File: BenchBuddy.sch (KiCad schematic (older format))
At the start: 0 parts

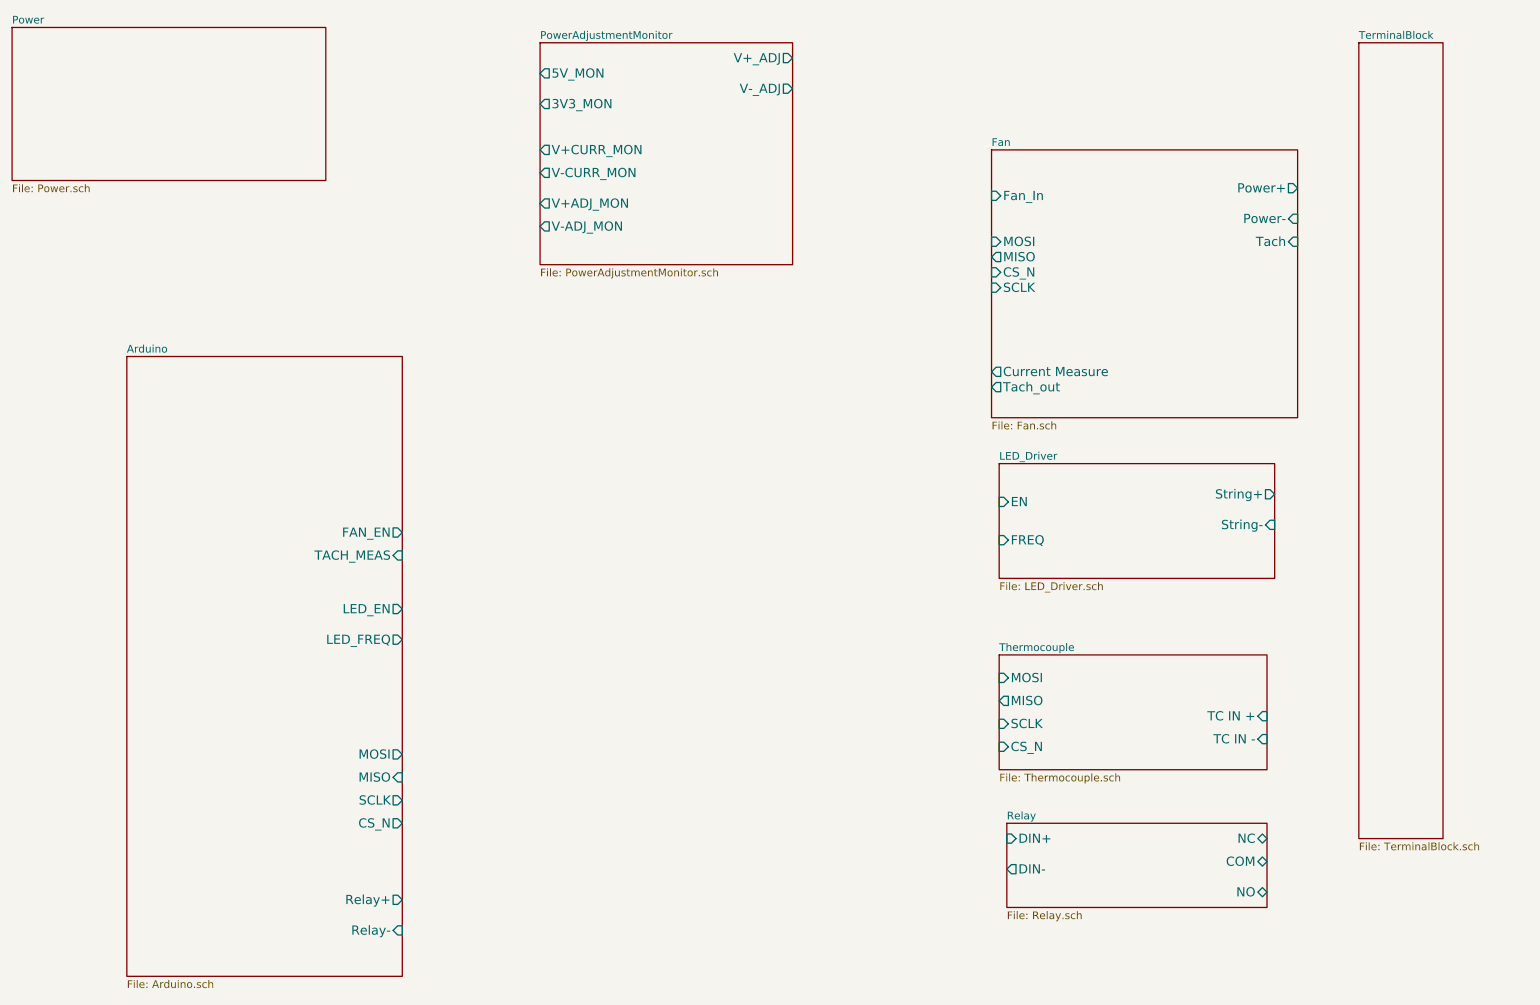
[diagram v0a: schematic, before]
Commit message: Changes up to and including Arduino module
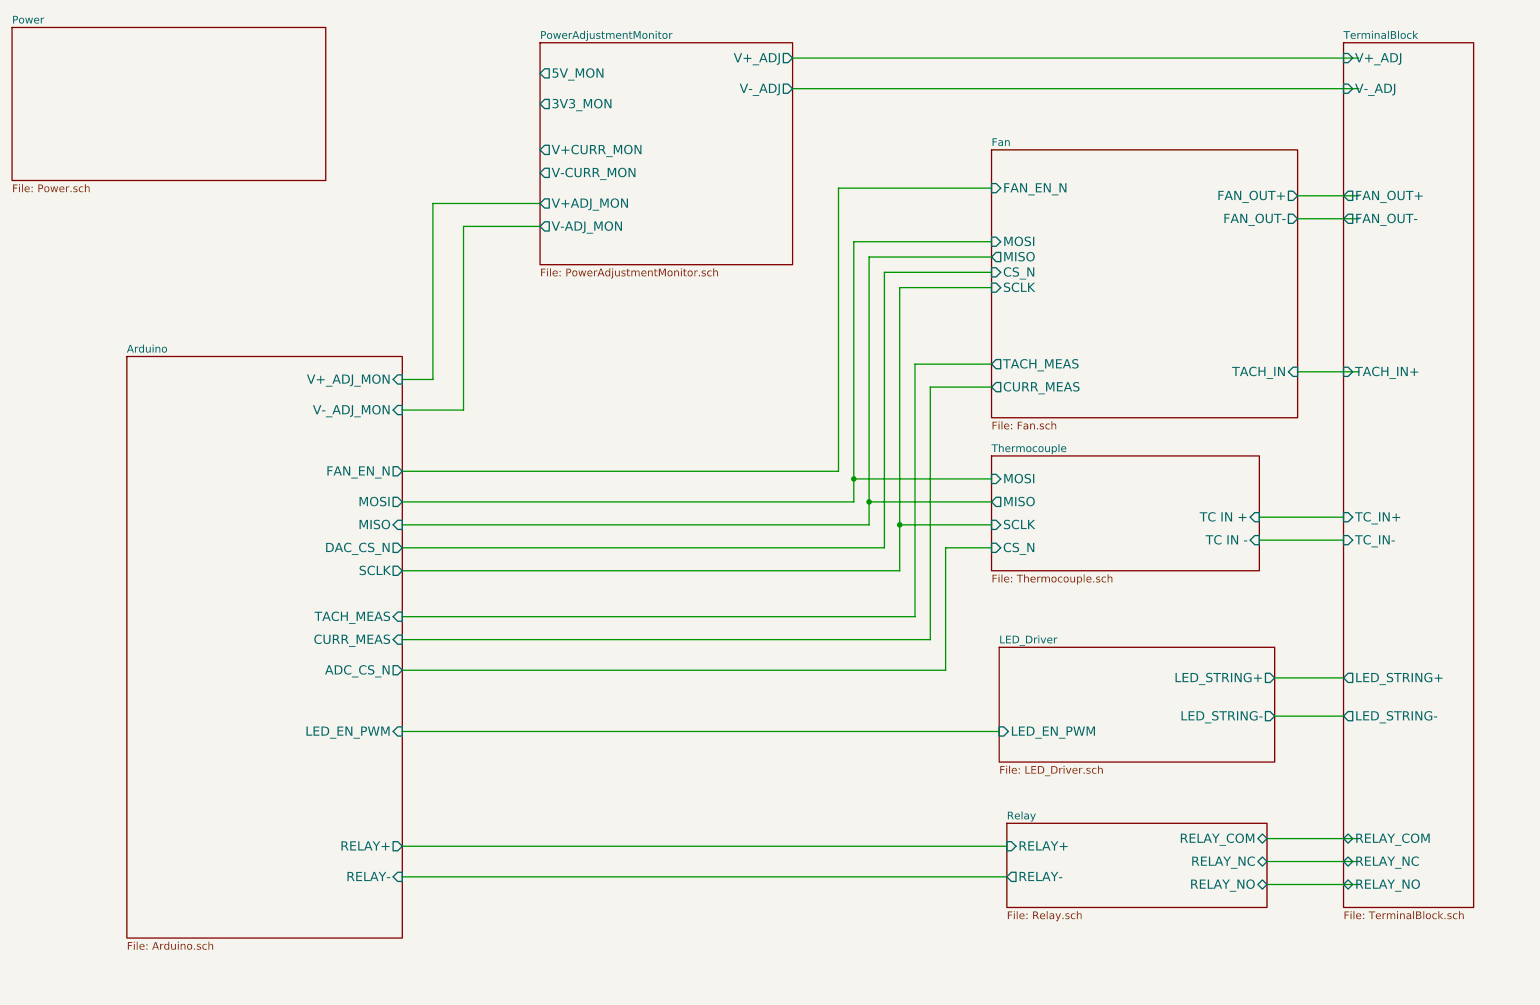
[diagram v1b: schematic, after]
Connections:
- wire segments 0 -> 48
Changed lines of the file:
@@
 LIBS:valves
 LIBS:BencyBuddy
+LIBS:arduino_shieldsNCL
 LIBS:BenchBuddy-cache
 EELAYER 27 0
@@
 Sheet 1 9
 Title ""
-Date "9 feb 2014"
+Date "12 feb 2014"
 Rev ""
 Comp ""
@@
 $EndDescr
 $Sheet
-S 1850 3200 1800 4050
+S 1850 3200 1800 3800
 U 52EF15C4
 F0 "Arduino" 50
 F1 "Arduino.sch" 50
-F2 "Relay+" O R 3650 6750 60
-F3 "Relay-" I R 3650 6950 60
-F4 "MOSI" O R 3650 5800 60
-F5 "MISO" I R 3650 5950 60
-F6 "SCLK" O R 3650 6100 60
-F7 "CS_N" O R 3650 6250 60
-F8 "LED_EN" O R 3650 4850 60
-F9 "LED_FREQ" O R 3650 5050 60
-F10 "FAN_EN" O R 3650 4350 60
-F11 "TACH_MEAS" I R 3650 4500 60
+F2 "RELAY+" O R 3650 6400 60
+F3 "RELAY-" I R 3650 6600 60
+F4 "MOSI" O R 3650 4150 60
+F5 "MISO" I R 3650 4300 60
+F6 "SCLK" O R 3650 4600 60
+F7 "TACH_MEAS" I R 3650 4900 60
+F8 "FAN_EN_N" O R 3650 3950 60
+F9 "CURR_MEAS" I R 3650 5050 60
+F10 "V+_ADJ_MON" I R 3650 3350 60
+F11 "V-_ADJ_MON" I R 3650 3550 60
+F12 "LED_EN_PWM" I R 3650 5650 60
+F13 "DAC_CS_N" O R 3650 4450 60
+F14 "ADC_CS_N" O R 3650 5250 60
 $EndSheet
 $Sheet
@@
 F0 "Relay" 50
 F1 "Relay.sch" 50
-F2 "DIN+" I L 7600 6350 60
-F3 "DIN-" O L 7600 6550 60
-F4 "NC" B R 9300 6350 60
-F5 "NO" B R 9300 6700 60
-F6 "COM" B R 9300 6500 60
+F2 "RELAY_NC" B R 9300 6500 60
+F3 "RELAY_NO" B R 9300 6650 60
+F4 "RELAY_COM" B R 9300 6350 60
+F5 "RELAY+" I L 7600 6400 60
+F6 "RELAY-" O L 7600 6600 60
 $EndSheet
 $Sheet
@@
 $EndSheet
 $Sheet
-S 7550 3900 1800 750
-U 52EF16AC
-F0 "LED_Driver" 50
-F1 "LED_Driver.sch" 50
-F2 "EN" I L 7550 4150 60
-F3 "FREQ" I L 7550 4400 60
-F4 "String+" O R 9350 4100 60
-F5 "String-" I R 9350 4300 60
-$EndSheet
-$Sheet
 S 7500 1850 2000 1750
 U 52EF16C7
 F0 "Fan" 50
 F1 "Fan.sch" 50
-F2 "Power+" O R 9500 2100 60
-F3 "Power-" I R 9500 2300 60
-F4 "Tach" I R 9500 2450 60
-F5 "Tach_out" O L 7500 3400 60
-F6 "Fan_In" I L 7500 2150 60
-F7 "Current Measure" O L 7500 3300 60
-F8 "MOSI" I L 7500 2450 60
-F9 "MISO" O L 7500 2550 60
-F10 "CS_N" I L 7500 2650 60
-F11 "SCLK" I L 7500 2750 60
-$EndSheet
-$Sheet
-S 9900 1150 550  5200
-U 52EF16F4
-F0 "TerminalBlock" 50
-F1 "TerminalBlock.sch" 50
-$EndSheet
-$Sheet
-S 7550 5150 1750 750
+F2 "MOSI" I L 7500 2450 60
+F3 "MISO" O L 7500 2550 60
+F4 "CS_N" I L 7500 2650 60
+F5 "SCLK" I L 7500 2750 60
+F6 "FAN_OUT+" O R 9500 2150 60
+F7 "FAN_OUT-" O R 9500 2300 60
+F8 "TACH_IN" I R 9500 3300 60
+F9 "TACH_MEAS" O L 7500 3250 60
+F10 "FAN_EN_N" I L 7500 2100 60
+F11 "CURR_MEAS" O L 7500 3400 60
+$EndSheet
+$Sheet
+S 7500 3850 1750 750
 U 52EF176B
 F0 "Thermocouple" 50
 F1 "Thermocouple.sch" 50
-F2 "TC IN +" I R 9300 5550 60
-F3 "TC IN -" I R 9300 5700 60
-F4 "MOSI" I L 7550 5300 60
-F5 "MISO" O L 7550 5450 60
-F6 "SCLK" I L 7550 5600 60
-F7 "CS_N" I L 7550 5750 60
+F2 "TC IN +" I R 9250 4250 60
+F3 "TC IN -" I R 9250 4400 60
+F4 "MOSI" I L 7500 4000 60
+F5 "MISO" O L 7500 4150 60
+F6 "SCLK" I L 7500 4300 60
+F7 "CS_N" I L 7500 4450 60
 $EndSheet
 $Sheet
@@
 F9 "V-CURR_MON" O L 4550 2000 60
 $EndSheet
+Wire Wire Line
+	9500 2300 9900 2300
+Wire Wire Line
+	9900 2150 9500 2150
+Wire Wire Line
+	9900 1450 6200 1450
+Wire Wire Line
+	6200 1250 9900 1250
+Wire Wire Line
+	9900 3300 9500 3300
+$Sheet
+S 9800 1150 850  5650
+U 52EF16F4
+F0 "TerminalBlock" 50
+F1 "TerminalBlock.sch" 50
+F2 "V+_ADJ" I L 9800 1250 60
+F3 "V-_ADJ" I L 9800 1450 60
+F4 "FAN_OUT+" O L 9800 2150 60
+F5 "FAN_OUT-" O L 9800 2300 60
+F6 "TACH_IN+" I L 9800 3300 60
+F7 "LED_STRING+" O L 9800 5300 60
+F8 "LED_STRING-" O L 9800 5550 60
+F9 "TC_IN+" I L 9800 4250 60
+F10 "TC_IN-" I L 9800 4400 60
+F11 "RELAY_COM" B L 9800 6350 60
+F12 "RELAY_NC" B L 9800 6500 60
+F13 "RELAY_NO" B L 9800 6650 60
+$EndSheet
+Wire Wire Line
+	9300 6350 9900 6350
+Wire Wire Line
+	9900 6500 9300 6500
+Wire Wire Line
+	9300 6650 9900 6650
+Wire Wire Line
+	3650 3350 3850 3350
+Wire Wire Line
+	3850 3350 3850 2200
+Wire Wire Line
+	3850 2200 4550 2200
+Wire Wire Line
+	3650 3550 4050 3550
+Wire Wire Line
+	4050 3550 4050 2350
+Wire Wire Line
+	4050 2350 4550 2350
+Wire Wire Line
+	3650 3950 6500 3950
+Wire Wire Line
+	6500 3950 6500 2100
+Wire Wire Line
+	6500 2100 7500 2100
+Wire Wire Line
+	3650 4150 6600 4150
+Wire Wire Line
+	6600 4150 6600 2450
+Wire Wire Line
+	6600 2450 7500 2450
+Wire Wire Line
+	7500 2550 6700 2550
+Wire Wire Line
+	6700 2550 6700 4300
+Wire Wire Line
+	6700 4300 3650 4300
+Wire Wire Line
+	7500 2650 6800 2650
+Wire Wire Line
+	6800 2650 6800 4450
+Wire Wire Line
+	6800 4450 3650 4450
+Wire Wire Line
+	3650 4600 6900 4600
+Wire Wire Line
+	6900 4600 6900 2750
+Wire Wire Line
+	6900 2750 7500 2750
+Wire Wire Line
+	7500 3250 7000 3250
+Wire Wire Line
+	7000 3250 7000 4900
+Wire Wire Line
+	7000 4900 3650 4900
+Wire Wire Line
+	3650 5050 7100 5050
+Wire Wire Line
+	7100 5050 7100 3400
+Wire Wire Line
+	7100 3400 7500 3400
+$Sheet
+S 7550 5100 1800 750
+U 52EF16AC
+F0 "LED_Driver" 50
+F1 "LED_Driver.sch" 50
+F2 "LED_EN_PWM" I L 7550 5650 60
+F3 "LED_STRING+" O R 9350 5300 60
+F4 "LED_STRING-" O R 9350 5550 60
+$EndSheet
+Wire Wire Line
+	7500 4450 7200 4450
+Wire Wire Line
+	7200 4450 7200 5250
+Wire Wire Line
+	7200 5250 3650 5250
+Wire Wire Line
+	7550 5650 3650 5650
+Wire Wire Line
+	7500 4300 6900 4300
+Connection ~ 6900 4300
+Wire Wire Line
+	7500 4150 6700 4150
+Connection ~ 6700 4150
+Wire Wire Line
+	7500 4000 6600 4000
+Connection ~ 6600 4000
+Wire Wire Line
+	3650 6400 7600 6400
+Wire Wire Line
+	7600 6600 3650 6600
+Wire Wire Line
+	9800 4250 9250 4250
+Wire Wire Line
+	9250 4400 9800 4400
+Wire Wire Line
+	9800 5300 9350 5300
+Wire Wire Line
+	9350 5550 9800 5550
 $EndSCHEMATC

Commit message: Current/Fan updates
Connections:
- wire segments 48 -> 51
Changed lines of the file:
@@
 Sheet 1 9
 Title ""
-Date "12 feb 2014"
+Date "13 feb 2014"
 Rev ""
 Comp ""
@@
 Comment4 ""
 $EndDescr
-$Sheet
-S 1850 3200 1800 3800
-U 52EF15C4
-F0 "Arduino" 50
-F1 "Arduino.sch" 50
-F2 "RELAY+" O R 3650 6400 60
-F3 "RELAY-" I R 3650 6600 60
-F4 "MOSI" O R 3650 4150 60
-F5 "MISO" I R 3650 4300 60
-F6 "SCLK" O R 3650 4600 60
-F7 "TACH_MEAS" I R 3650 4900 60
-F8 "FAN_EN_N" O R 3650 3950 60
-F9 "CURR_MEAS" I R 3650 5050 60
-F10 "V+_ADJ_MON" I R 3650 3350 60
-F11 "V-_ADJ_MON" I R 3650 3550 60
-F12 "LED_EN_PWM" I R 3650 5650 60
-F13 "DAC_CS_N" O R 3650 4450 60
-F14 "ADC_CS_N" O R 3650 5250 60
-$EndSheet
 $Sheet
 S 7600 6250 1700 550
@@
 F8 "TACH_IN" I R 9500 3300 60
 F9 "TACH_MEAS" O L 7500 3250 60
-F10 "FAN_EN_N" I L 7500 2100 60
-F11 "CURR_MEAS" O L 7500 3400 60
+F10 "CURR_MEAS" O L 7500 3400 60
+F11 "FAN_MODE" I L 7500 2000 60
+F12 "FAN_PWM" I L 7500 2200 60
 $EndSheet
 $Sheet
@@
 	3650 3950 6500 3950
 Wire Wire Line
-	6500 3950 6500 2100
-Wire Wire Line
-	6500 2100 7500 2100
-Wire Wire Line
-	3650 4150 6600 4150
-Wire Wire Line
-	6600 4150 6600 2450
+	6500 3950 6500 2200
+Wire Wire Line
+	6500 2200 7500 2200
+Wire Wire Line
+	6600 4150 3650 4150
+Wire Wire Line
+	6600 2450 6600 4150
 Wire Wire Line
 	6600 2450 7500 2450
@@
 	6800 4450 3650 4450
 Wire Wire Line
-	3650 4600 6900 4600
-Wire Wire Line
-	6900 4600 6900 2750
+	6900 4600 3650 4600
+Wire Wire Line
+	6900 2750 6900 4600
 Wire Wire Line
 	6900 2750 7500 2750
@@
 Wire Wire Line
 	9350 5550 9800 5550
+Wire Wire Line
+	3650 3750 6350 3750
+Wire Wire Line
+	6350 3750 6350 2000
+Wire Wire Line
+	6350 2000 7500 2000
+$Sheet
+S 1850 3200 1800 3800
+U 52EF15C4
+F0 "Arduino" 50
+F1 "Arduino.sch" 50
+F2 "RELAY+" O R 3650 6400 60
+F3 "MOSI" O R 3650 4150 60
+F4 "MISO" I R 3650 4300 60
+F5 "SCLK" O R 3650 4600 60
+F6 "TACH_MEAS" I R 3650 4900 60
+F7 "CURR_MEAS" I R 3650 5050 60
+F8 "V+_ADJ_MON" I R 3650 3350 60
+F9 "V-_ADJ_MON" I R 3650 3550 60
+F10 "LED_EN_PWM" I R 3650 5650 60
+F11 "DAC_CS_N" O R 3650 4450 60
+F12 "ADC_CS_N" O R 3650 5250 60
+F13 "FAN_MODE" I R 3650 3750 60
+F14 "FAN_PWM" O R 3650 3950 60
+F15 "RELAY-" I R 3650 6600 60
+$EndSheet
 $EndSCHEMATC
